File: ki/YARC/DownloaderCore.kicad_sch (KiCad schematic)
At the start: 13 parts, among them J1 NANOIO_EXT, J2 MCR_EXT, J3 PULSE_EXT, U1 74HCT574, U2 74HCT574, U3 74HCT574, U4 74HCT574, U5 74HCT574, U6 74LS138, U7 74HCT574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

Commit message: Continuing cleanup of schematic
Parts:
- removed J1: NANOIO_EXT, symbol Connector_Generic:Conn_01x08
- removed J2: MCR_EXT, symbol Connector_Generic:Conn_01x04
- removed J3: PULSE_EXT, symbol Connector_Generic:Conn_01x04
- removed U8: 74HC245, symbol 74xx:74HC245
- added U148: 74HC245, symbol 74xx:74HC245
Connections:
- net MCR.YARC_NANO# is gone; now on net YARC/~{NANO}: U7.14 (Q5)
- net GND: now also U148.10 (GND)
- net MCR.FASTCLK_EN#: now also U148.5 (A3)
- net MCR.IR_EN#: now also U148.8 (A6)
- net MCR.REG_WR_EN#: now also U148.2 (A0)
- net MCR.SVC_STATUS: now also U148.3 (A1); no longer U7.13 (Q6)
- net MCR.SYSBUS_EN#: now also U148.7 (A5)
- net MCR.WCS_EN#: now also U148.9 (A7)
- net NANOIO0: now also U148.18 (B0)
- net NANOIO1: now also U148.17 (B1)
- net NANOIO2: now also U148.16 (B2)
- net NANOIO3: now also U148.15 (B3)
- net NANOIO4: now also U148.14 (B4)
- net NANOIO5: now also U148.13 (B5)
- net NANOIO6: now also U148.12 (B6)
- net NANOIO7: now also U148.11 (B7)
- net VCC: now also U148.1 (A->B), U148.20 (VCC)
- net YARC/~{NANO}: now also U148.4 (A2)
- net ~{MCR_IN}: now reaches U6.10 (O5)
- net ~{MCR_IN}: now also U148.19 (CE)
- net RESET_SERVICE: now reaches U9.11 (O4)
- net RAW_NANO_CLK: now reaches U9.10 (O5)
- net DISP_CLK: now reaches U9.9 (O6)
- net MCR.POR_SENSE: no longer names the net of U7.16 (Q3)
- net MCRCLK renamed MCR_CLK
- net SYSCLK7 renamed SYSCLK
- new net ~{POR3}: U148.6 (A4)
- no-connect marks 19 -> 20
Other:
- note added: "MCR"
- note removed: "WW connector at top of board"
- moved on the sheet: U7

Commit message: Ongoing schematic changes
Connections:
- net ~{UC_RAM_EN_OUT}: now reaches U9.12 (O3)
- net ~{UC_RAM_DIS_OUT}: now reaches U9.13 (O2)
- no-connect marks 20 -> 18
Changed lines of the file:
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@@
   (no_connect (at 114.3 124.46))
   (no_connect (at 124.46 134.62))
-  (no_connect (at 218.44 134.62))
   (no_connect (at 109.22 124.46))
   (no_connect (at 165.1 121.92))
   (no_connect (at 124.46 165.1))
   (no_connect (at 99.06 139.7))
-  (no_connect (at 218.44 137.16))
   (no_connect (at 124.46 167.64))
   (no_connect (at 99.06 142.24))
@@
     (stroke (width 0) (type default))
   )
+  (wire (pts (xy 218.44 137.16) (xy 223.52 137.16))
+    (stroke (width 0) (type default))
+  )
   (wire (pts (xy 76.2 157.48) (xy 99.06 157.48))
     (stroke (width 0) (type default))
@@
     (stroke (width 0) (type default))
   )
+  (wire (pts (xy 218.44 134.62) (xy 223.52 134.62))
+    (stroke (width 0) (type default))
+  )
   (bus (pts (xy 162.56 38.1) (xy 162.56 40.64))
     (stroke (width 0) (type default))
@@
     (effects (font (size 1.27 1.27)) (justify left bottom))
   )
-  (label "NANOIO7" (at 165.1 38.1 0)
+  (label "NANOIO7" (at 165.1 38.1 0) (fields_autoplaced)
     (effects (font (size 1.27 1.27)) (justify left bottom))
   )
@@
     (effects (font (size 1.27 1.27)) (justify left bottom))
   )
-  (label "NANOIO3" (at 165.1 48.26 0)
+  (label "NANOIO3" (at 165.1 48.26 0) (fields_autoplaced)
     (effects (font (size 1.27 1.27)) (justify left bottom))
   )
@@
     (effects (font (size 1.27 1.27)) (justify left bottom))
   )
-  (label "MCR.POR_SENSE" (at 231.14 45.72 0)
+  (label "MCR.POR_SENSE" (at 231.14 45.72 0) (fields_autoplaced)
     (effects (font (size 1.27 1.27)) (justify left bottom))
   )
@@
     (effects (font (size 1.27 1.27)) (justify right bottom))
   )
-  (label "NANOIO5" (at 165.1 43.18 0)
+  (label "NANOIO5" (at 165.1 43.18 0) (fields_autoplaced)
     (effects (font (size 1.27 1.27)) (justify left bottom))
   )
@@
     (effects (font (size 1.27 1.27)) (justify left bottom))
   )
-  (label "MCR.SYSBUS_EN#" (at 207.01 43.18 0)
+  (label "MCR.SYSBUS_EN#" (at 207.01 43.18 0) (fields_autoplaced)
     (effects (font (size 1.27 1.27)) (justify left bottom))
   )
@@
     (effects (font (size 1.27 1.27)) (justify left bottom))
   )
-  (label "NANOIO4" (at 165.1 45.72 0)
+  (label "NANOIO4" (at 165.1 45.72 0) (fields_autoplaced)
     (effects (font (size 1.27 1.27)) (justify left bottom))
   )
@@
     (effects (font (size 1.27 1.27)) (justify left bottom))
   )
-  (label "MCR.REG_WR_EN#" (at 207.01 55.88 0)
+  (label "MCR.REG_WR_EN#" (at 207.01 55.88 0) (fields_autoplaced)
     (effects (font (size 1.27 1.27)) (justify left bottom))
   )
@@
     (effects (font (size 1.27 1.27)) (justify left bottom))
   )
-  (label "MCR.POR_SENSE" (at 207.01 45.72 0)
+  (label "MCR.POR_SENSE" (at 207.01 45.72 0) (fields_autoplaced)
     (effects (font (size 1.27 1.27)) (justify left bottom))
   )
@@
     (effects (font (size 1.27 1.27)) (justify left bottom))
   )
-  (label "NANOIO1" (at 165.1 53.34 0)
-    (effects (font (size 1.27 1.27)) (justify left bottom))
-  )
-  (label "NANOIO0" (at 165.1 55.88 0)
+  (label "NANOIO1" (at 165.1 53.34 0) (fields_autoplaced)
+    (effects (font (size 1.27 1.27)) (justify left bottom))
+  )
+  (label "NANOIO0" (at 165.1 55.88 0) (fields_autoplaced)
     (effects (font (size 1.27 1.27)) (justify left bottom))
   )
@@
     (effects (font (size 1.27 1.27)) (justify left bottom))
   )
-  (label "NANOIO6" (at 165.1 40.64 0)
+  (label "NANOIO6" (at 165.1 40.64 0) (fields_autoplaced)
     (effects (font (size 1.27 1.27)) (justify left bottom))
   )
@@
     (effects (font (size 1.27 1.27)) (justify right bottom))
   )
-  (label "MCR.YARC_NANO#" (at 231.14 87.63 0)
-    (effects (font (size 1.27 1.27)) (justify left bottom))
-  )
-  (label "NANOIO2" (at 165.1 50.8 0)
+  (label "MCR.YARC_NANO#" (at 231.14 87.63 0) (fields_autoplaced)
+    (effects (font (size 1.27 1.27)) (justify left bottom))
+  )
+  (label "NANOIO2" (at 165.1 50.8 0) (fields_autoplaced)
     (effects (font (size 1.27 1.27)) (justify left bottom))
   )
@@
     (effects (font (size 1.27 1.27)) (justify right bottom))
   )
-  (label "MCR.SVC_STATUS" (at 207.01 53.34 0)
+  (label "MCR.SVC_STATUS" (at 207.01 53.34 0) (fields_autoplaced)
     (effects (font (size 1.27 1.27)) (justify left bottom))
   )
@@
     (effects (font (size 1.27 1.27)) (justify left bottom))
   )
-  (label "MCR.IR_EN#" (at 207.01 40.64 0)
+  (label "MCR.IR_EN#" (at 207.01 40.64 0) (fields_autoplaced)
     (effects (font (size 1.27 1.27)) (justify left bottom))
   )
@@
     (effects (font (size 1.27 1.27)) (justify left bottom))
   )
-  (label "MCR.YARC_NANO#" (at 207.01 50.8 0)
+  (label "MCR.YARC_NANO#" (at 207.01 50.8 0) (fields_autoplaced)
     (effects (font (size 1.27 1.27)) (justify left bottom))
   )
@@
     (effects (font (size 1.27 1.27)) (justify right bottom))
   )
-  (label "MCR.WCS_EN#" (at 207.01 38.1 0)
+  (label "MCR.WCS_EN#" (at 207.01 38.1 0) (fields_autoplaced)
     (effects (font (size 1.27 1.27)) (justify left bottom))
   )
@@
     (effects (font (size 1.27 1.27)) (justify left bottom))
   )
-  (label "MCR.FASTCLK_EN#" (at 207.01 48.26 0)
+  (label "MCR.FASTCLK_EN#" (at 207.01 48.26 0) (fields_autoplaced)
     (effects (font (size 1.27 1.27)) (justify left bottom))
   )
@@
     )
   )
+  (global_label "~{UC_RAM_EN_OUT}" (shape input) (at 223.52 137.16 0) (fields_autoplaced)
+    (effects (font (size 1.27 1.27)) (justify left))
+    (property "Intersheetrefs" "${INTERSHEET_REFS}" (at 241.3545 137.0806 0)
+      (effects (font (size 1.27 1.27)) (justify left) hide)
+    )
+  )
   (global_label "SYSADDR[0..15]" (shape input) (at 15.24 43.18 90) (fields_autoplaced)
     (effects (font (size 1.27 1.27)) (justify left))
@@
       (effects (font (size 1.27 1.27)) (justify left) hide)
     )
+  )
+  (global_label "~{UC_RAM_DIS_OUT}" (shape input) (at 223.52 134.62 0) (fields_autoplaced)
+    (effects (font (size 1.27 1.27)) (justify left))
+    (property "Intersheetrefs" "${INTERSHEET_REFS}" (at 241.9593 134.5406 0)
+      (effects (font (size 1.27 1.27)) (justify left) hide)
+    )

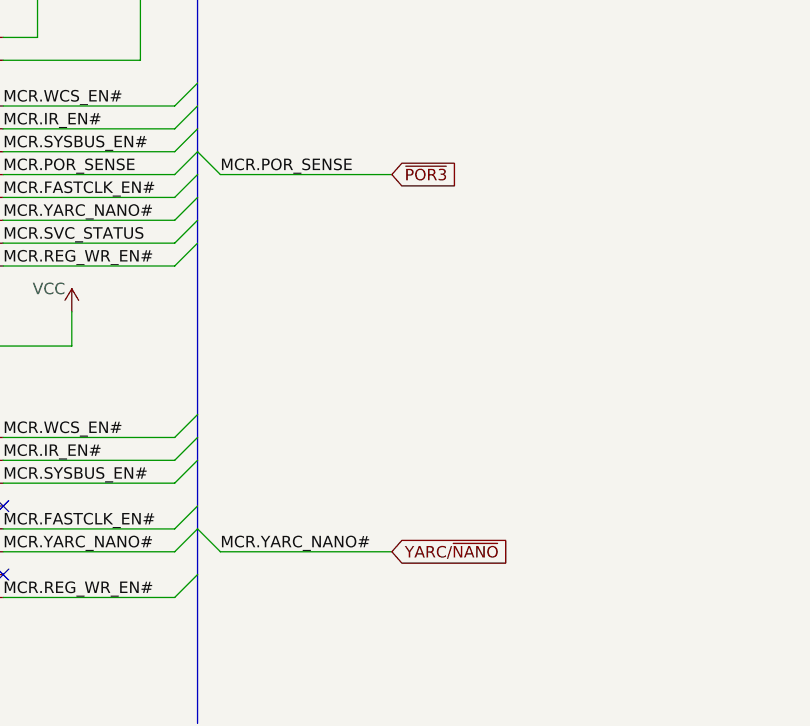
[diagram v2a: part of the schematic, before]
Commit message: Schematic for addressing unit is complete and all ERC violations addressed
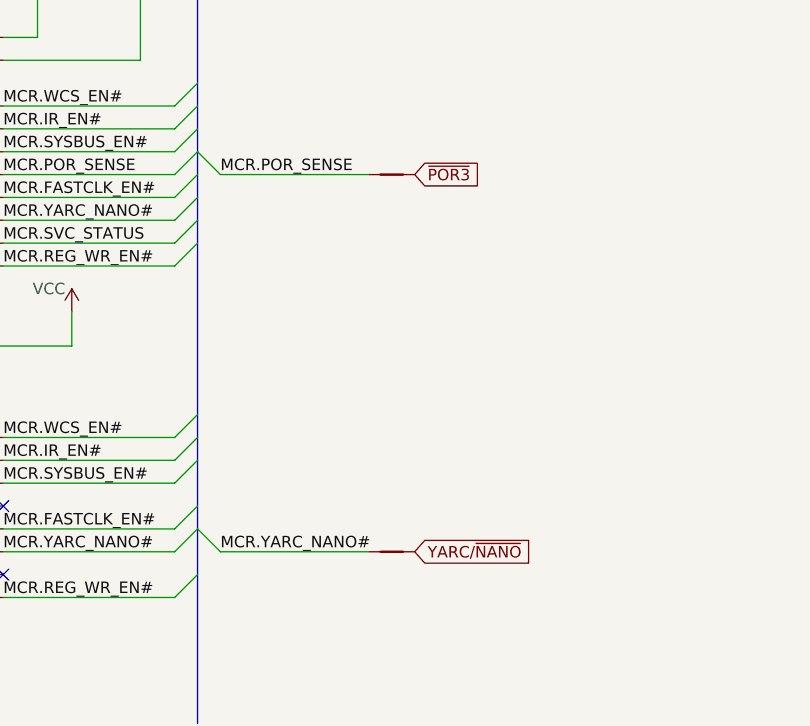
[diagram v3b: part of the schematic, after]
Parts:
- added NT155, NT156: NetTie_2, symbol Device:NetTie_2
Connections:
- net YARC/~{NANO}: now also NT156.2; no longer U148.4 (A2), U7.14 (Q5)
- net ~{POR3}: now also NT155.2; no longer U148.6 (A4)
- new net MCR.POR_SENSE: NT155.1, U148.6 (A4)
- new net MCR.YARC_NANO#: NT156.1, U148.4 (A2), U7.14 (Q5)
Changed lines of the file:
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@@
     (stroke (width 0) (type default))
   )
-  (wire (pts (xy 231.14 45.72) (xy 250.19 45.72))
+  (wire (pts (xy 231.14 45.72) (xy 247.65 45.72))
     (stroke (width 0) (type default))
   )
@@
     (stroke (width 0) (type default))
   )
-  (wire (pts (xy 231.14 87.63) (xy 250.19 87.63))
+  (wire (pts (xy 231.14 87.63) (xy 247.65 87.63))
     (stroke (width 0) (type default))
   )
@@
     )
   )
+  (global_label "~{POR3}" (shape input) (at 252.73 45.72 0) (fields_autoplaced)
+    (effects (font (size 1.27 1.27)) (justify left))
+    (property "Intersheetrefs" "${INTERSHEET_REFS}" (at 260.7952 45.72 0)
+      (effects (font (size 1.27 1.27)) (justify left) hide)
+    )
+  )
   (global_label "~{UC_RAM_DIS_OUT}" (shape input) (at 223.52 134.62 0) (fields_autoplaced)
     (effects (font (size 1.27 1.27)) (justify left))
@@
     )
   )
-  (global_label "~{POR3}" (shape input) (at 250.19 45.72 0) (fields_autoplaced)
-    (effects (font (size 1.27 1.27)) (justify left))
-    (property "Intersheetrefs" "${INTERSHEET_REFS}" (at 258.2552 45.72 0)
-      (effects (font (size 1.27 1.27)) (justify left) hide)
-    )
-  )
   (global_label "NANOIO[0..7]" (shape input) (at 166.37 17.78 0) (fields_autoplaced)
     (effects (font (size 1.27 1.27)) (justify left))
@@
     )
   )
-  (global_label "YARC{slash}~{NANO}" (shape input) (at 250.19 87.63 0) (fields_autoplaced)
+  (global_label "YARC{slash}~{NANO}" (shape input) (at 252.73 87.63 0) (fields_autoplaced)
     (effects (font (size 1.27 1.27)) (justify left))
-    (property "Intersheetrefs" "${INTERSHEET_REFS}" (at 264.303 87.63 0)
+    (property "Intersheetrefs" "${INTERSHEET_REFS}" (at 266.843 87.63 0)
       (effects (font (size 1.27 1.27)) (justify left) hide)
     )
@@
         )
       )
+    )
+  )
+  (symbol (lib_id "Device:NetTie_2") (at 250.19 45.72 0) (unit 1)
+    (in_bom no) (on_board yes) (dnp no) (fields_autoplaced)
+    (property "Reference" "NT155" (at 250.19 40.64 0)
+      (effects (font (size 1.27 1.27)) hide)
+    )
+    (property "Value" "NetTie_2" (at 250.19 43.18 0)
+      (effects (font (size 1.27 1.27)) hide)
+    )
+    (property "Footprint" "" (at 250.19 45.72 0)
+      (effects (font (size 1.27 1.27)) hide)
+    )
+    (property "Datasheet" "~" (at 250.19 45.72 0)
+      (effects (font (size 1.27 1.27)) hide)
+    )
+    (pin "1")
+    (pin "2")
+    (instances
+      (project "YARC"
+        (path "/22e0f8e1-b0d7-4d47-bb7c-8ef04cd95fca/baeeec1c-6d89-4b09-ba07-b183ebc66f47"
+          (reference "NT155") (unit 1)
+        )
+      )
+    )
+  )
+  (symbol (lib_id "Device:NetTie_2") (at 250.19 87.63 0) (unit 1)
+    (in_bom no) (on_board yes) (dnp no) (fields_autoplaced)
+    (property "Reference" "NT156" (at 250.19 82.55 0)
+      (effects (font (size 1.27 1.27)) hide)
+    )
+    (property "Value" "NetTie_2" (at 250.19 85.09 0)
+      (effects (font (size 1.27 1.27)) hide)
+    )
+    (property "Footprint" "" (at 250.19 87.63 0)
+      (effects (font (size 1.27 1.27)) hide)
+    )
+    (property "Datasheet" "~" (at 250.19 87.63 0)
+      (effects (font (size 1.27 1.27)) hide)
+    )
+    (pin "1")
+    (pin "2")
+    (instances
+      (project "YARC"
+        (path "/22e0f8e1-b0d7-4d47-bb7c-8ef04cd95fca/baeeec1c-6d89-4b09-ba07-b183ebc66f47"
+          (reference "NT156") (unit 1)
+        )
+      )

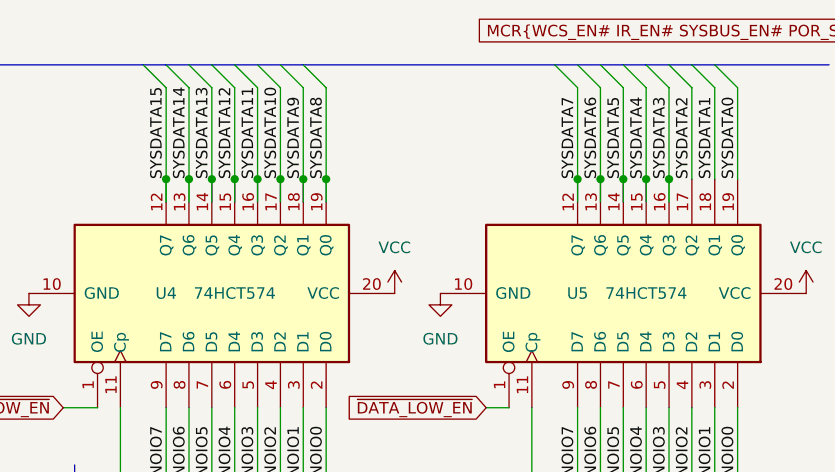
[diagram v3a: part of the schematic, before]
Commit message: Revise SET# logic for LD_UCODE_CTR#. Fix minor errors with no functional consequences (schematic didn't match reality)
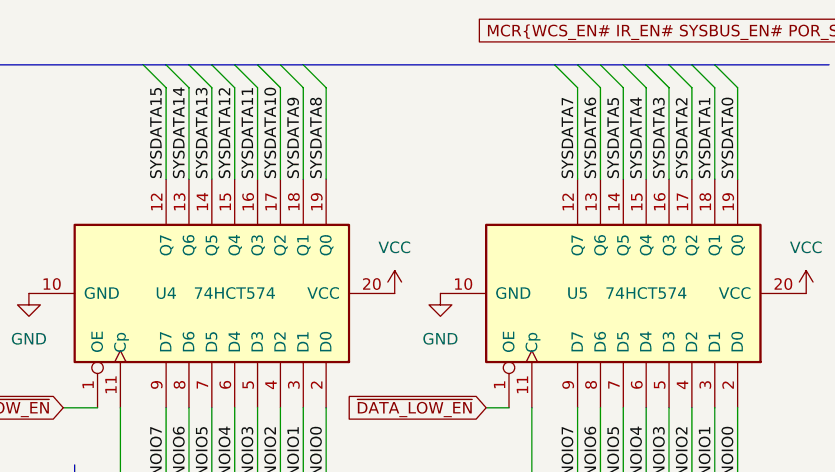
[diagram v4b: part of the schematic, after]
